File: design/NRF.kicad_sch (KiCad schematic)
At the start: 16 parts, among them U4 nRF24L01P, X2 16M

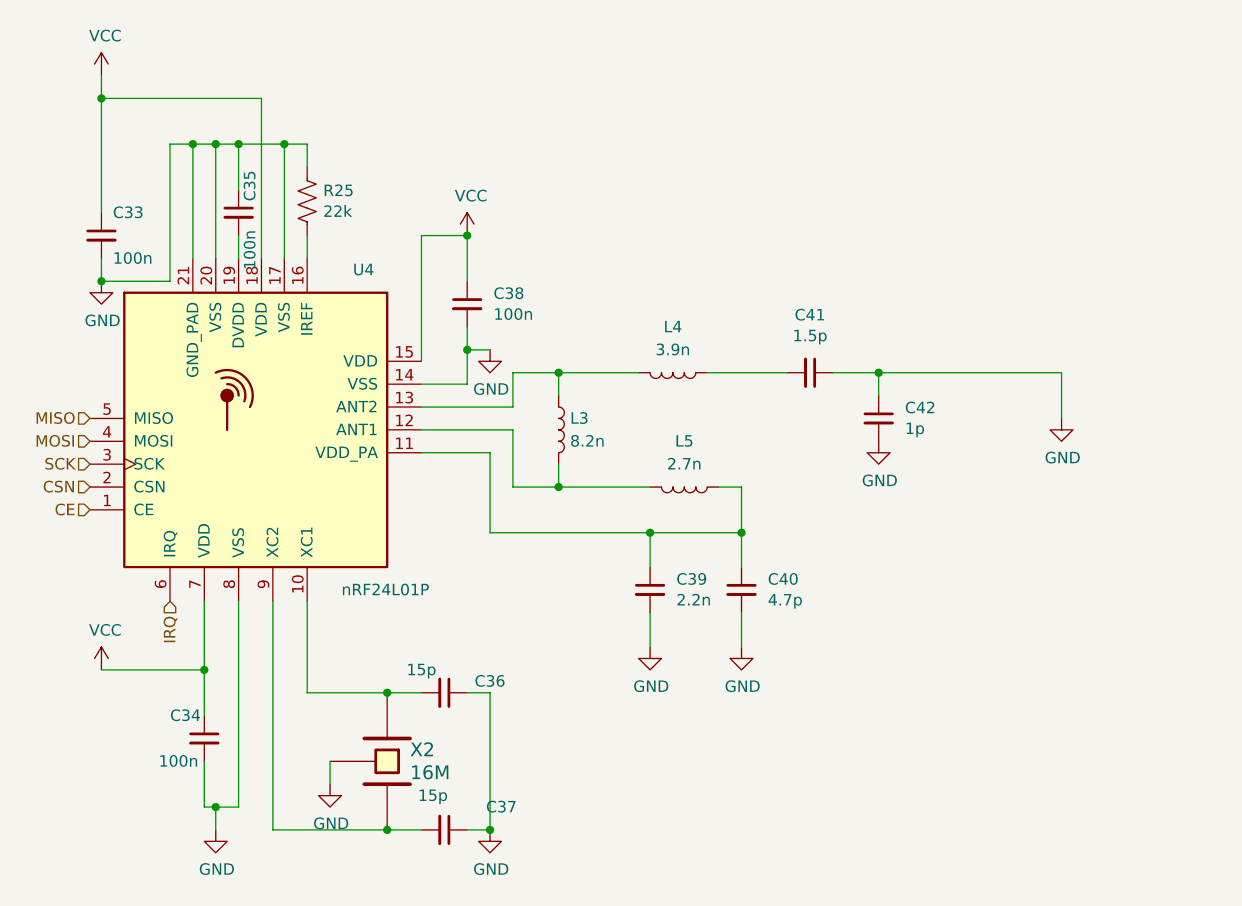
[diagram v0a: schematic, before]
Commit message: Impresión de esquemático en pdf
Impresión de la versión del esquemático en la carpeta /pdf
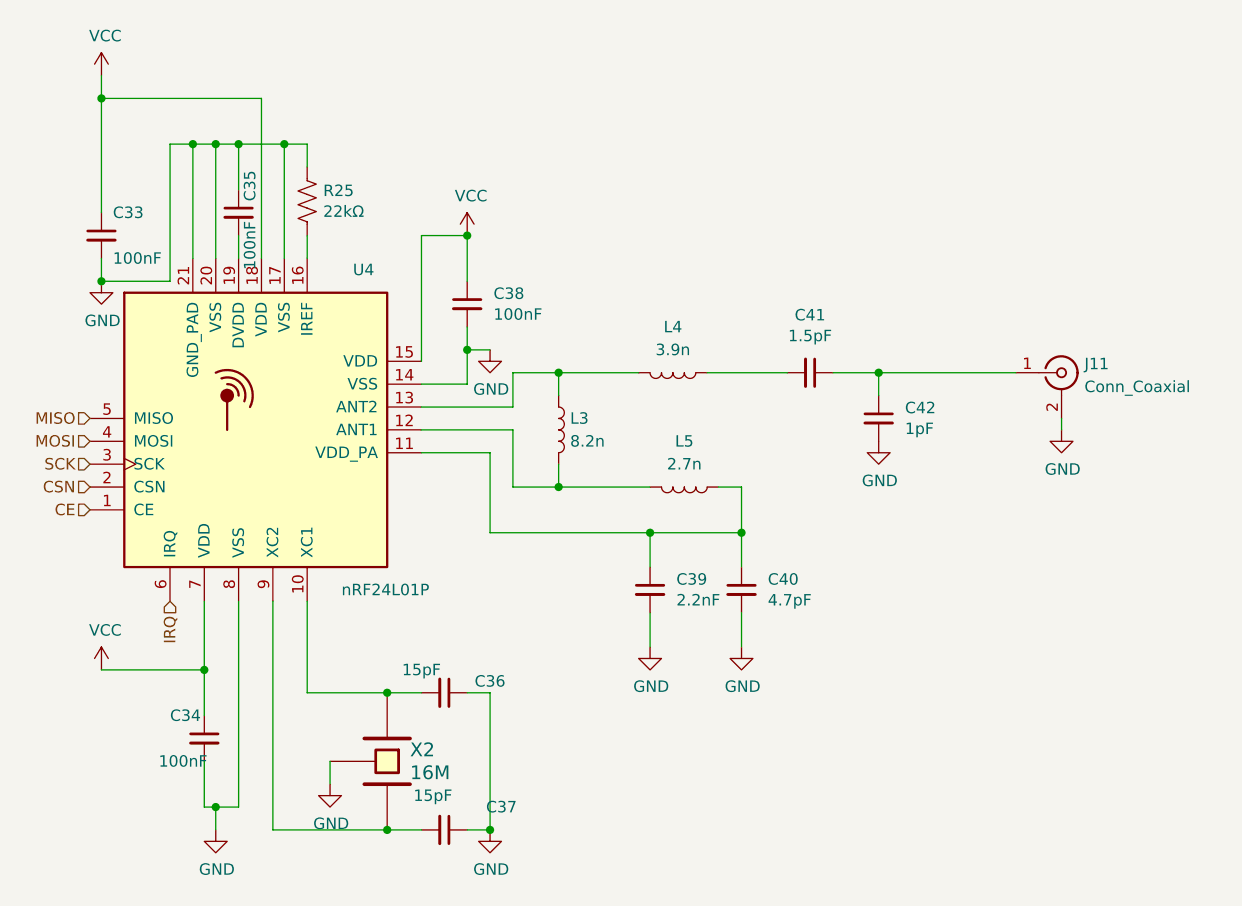
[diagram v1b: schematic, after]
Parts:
- added J11: Conn_Coaxial, symbol Connector:Conn_Coaxial
- C33, C34, C35, C38: value 100n -> 100nF
- C36, C37: value 15p -> 15pF
- C39: value 2.2n -> 2.2nF
- C40: value 4.7p -> 4.7pF
- C41: value 1.5p -> 1.5pF
- C42: value 1p -> 1pF
- R25: value 22k -> 22kΩ
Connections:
- net GND: now also J11.2 (Ext); no longer C41.1, C42.1
- new net: C41.1, C42.1, J11.1 (In)
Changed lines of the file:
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@@
-	(wire
-		(pts
-			(xy 238.76 73.66) (xy 238.76 78.74)
-		)
-		(stroke
-			(width 0)
-			(type default)
-		)
-	)
 	(wire
 		(pts
@@
 	(wire
 		(pts
+			(xy 238.76 80.01) (xy 238.76 78.74)
+		)
+		(stroke
+			(width 0)
+			(type default)
+		)
+	)
+	(wire
+		(pts
 			(xy 152.4 48.26) (xy 154.94 48.26)
 		)
@@
 	(wire
 		(pts
-			(xy 218.44 73.66) (xy 238.76 73.66)
+			(xy 218.44 73.66) (xy 233.68 73.66)
 		)
 		(stroke
@@
 			)
 		)
-		(property "Value" "100n"
+		(property "Value" "100nF"
 			(at 138.43 116.84 0)
 			(effects
@@
 			)
 		)
-		(property "Value" "15p"
+		(property "Value" "15pF"
 			(at 167.64 106.68 90)
 			(effects
@@
 			)
 		)
-		(property "Value" "15p"
+		(property "Value" "15pF"
 			(at 168.91 120.65 90)
 			(effects
@@
 			)
 		)
-		(property "Value" "2.2n"
+		(property "Value" "2.2nF"
 			(at 195.961 98.933 0)
 			(effects
@@
 			)
 		)
-		(property "Description" ""
+		(property "Description" "CAP CER 0603 2.2nF 16V X7R 10%"
 			(at 193.04 97.79 0)
 			(effects
@@
 			)
 		)
-		(property "Value" "4.7p"
+		(property "Value" "4.7pF"
 			(at 206.121 98.933 0)
 			(effects
@@
 			)
 		)
-		(property "Description" ""
+		(property "Description" "CAP CER 0603 4.7PF 16V X7R 10%"
 			(at 203.2 97.79 0)
 			(effects
@@
 			)
 		)
-		(property "Value" "1p"
+		(property "Value" "1pF"
 			(at 221.361 79.883 0)
 			(effects
@@
 			)
 		)
-		(property "Description" ""
+		(property "Description" "CAP CER 0603 1PF 16V X7R 10%"
 			(at 218.44 78.74 0)
 			(effects
@@
 			)
 		)
-		(property "Value" "1.5p"
+		(property "Value" "1.5pF"
 			(at 210.82 69.5706 90)
 			(effects
@@
 			)
 		)
-		(property "Description" ""
+		(property "Description" "CAP CER 0603 1.5PF 16V X7R 10%"
 			(at 210.82 73.66 0)
 			(effects
@@
 			)
 		)
-		(property "Value" "100n"
+		(property "Value" "100nF"
 			(at 175.641 67.183 0)
 			(effects
@@
 			)
 		)
-		(property "Value" "100n"
+		(property "Value" "100nF"
 			(at 133.35 60.96 0)
 			(effects
@@
 			)
 		)
-		(property "Value" "100n"
+		(property "Value" "100nF"
 			(at 148.59 62.23 90)
 			(effects
@@
 			)
 		)
-		(property "Value" "22k"
+		(property "Value" "22kΩ"
 			(at 156.718 55.753 0)
 			(effects
@@
 	(symbol
 		(lib_id "power:GND")
-		(at 238.76 78.74 0)
+		(at 238.76 80.01 0)
 		(unit 1)
 		(exclude_from_sim no)
@@
 		(dnp no)
 		(property "Reference" "#PWR068"
-			(at 238.76 85.09 0)
+			(at 238.76 86.36 0)
 			(effects
 				(font
@@
 		)
 		(property "Value" "GND"
-			(at 238.887 83.1342 0)
+			(at 238.887 84.4042 0)
 			(effects
 				(font
@@
 		)
 		(property "Footprint" ""
-			(at 238.76 78.74 0)
+			(at 238.76 80.01 0)
 			(effects
 				(font
@@
 		)
 		(property "Datasheet" ""
-			(at 238.76 78.74 0)
+			(at 238.76 80.01 0)
 			(effects
 				(font
@@
 		)
 		(property "Description" "Power symbol creates a global label with name \"GND\" , ground"
-			(at 238.76 78.74 0)
+			(at 238.76 80.01 0)
 			(effects
 				(font
@@
 					(unit 1)
 				)
+			)
+		)
+	)
+	(symbol
+		(lib_id "Connector:Conn_Coaxial")
+		(at 238.76 73.66 0)
+		(unit 1)
+		(exclude_from_sim no)
+		(in_bom yes)
+		(on_board yes)
+		(dnp no)
+		(fields_autoplaced yes)
+		(property "Reference" "J11"
+			(at 241.3 72.6831 0)
+			(effects
+				(font
+					(size 1.27 1.27)
+				)
+				(justify left)
+			)
+		)
+		(property "Value" "Conn_Coaxial"
+			(at 241.3 75.2231 0)
+			(effects
+				(font
+					(size 1.27 1.27)
+				)
+				(justify left)
+			)
+		)
+		(property "Footprint" ""
+			(at 238.76 73.66 0)
+			(effects
+				(font
+					(size 1.27 1.27)
+				)
+				(hide yes)
+			)
+		)
+		(property "Datasheet" " ~"
+			(at 238.76 73.66 0)
+			(effects
+				(font
+					(size 1.27 1.27)
+				)
+				(hide yes)
+			)
+		)
+		(property "Description" "coaxial connector (BNC, SMA, SMB, SMC, Cinch/RCA, LEMO, ...)"
+			(at 238.76 73.66 0)
+			(effects
+				(font
+					(size 1.27 1.27)
+				)
+				(hide yes)
+			)
+		)
+		(pin "2"
+		)
+		(pin "1"
+		)
+		(instances
+			(project "ESCX"
+				(path "/6389d757-a1bd-4c0a-9d55-6114b19cc67a/00000000-0000-0000-0000-00005ae4952f"
+					(reference "J11")
+					(unit 1)
+				)

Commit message: Agregado de footprints
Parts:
- L3, L4, L5: footprint (none) -> Inductor_SMD:L_0603_1608Metric_Pad1.05x0.95mm_HandSolder
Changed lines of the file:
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@@
 			)
 		)
-		(property "Description" "CAP 15p, 100V, 0603 "
+		(property "Description" "CAP 15p, 100V, 0603"
 			(at 170.18 109.22 0)
 			(effects
@@
 			)
 		)
-		(property "Description" "CAP 15p, 100V, 0603 "
+		(property "Description" "CAP 15p, 100V, 0603"
 			(at 170.18 124.46 0)
 			(effects
@@
 			)
 		)
-		(property "Footprint" ""
+		(property "Footprint" "Inductor_SMD:L_0603_1608Metric_Pad1.05x0.95mm_HandSolder"
 			(at 182.88 80.01 0)
 			(effects
@@
 			)
 		)
-		(property "Footprint" ""
+		(property "Footprint" "Inductor_SMD:L_0603_1608Metric_Pad1.05x0.95mm_HandSolder"
 			(at 195.58 73.66 0)
 			(effects
@@
 			)
 		)
-		(property "Footprint" ""
+		(property "Footprint" "Inductor_SMD:L_0603_1608Metric_Pad1.05x0.95mm_HandSolder"
 			(at 196.85 86.36 0)
 			(effects
@@
 			)
 		)
-		(property "Datasheet" " ~"
+		(property "Datasheet" "~"
 			(at 238.76 73.66 0)
 			(effects

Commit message: Agrego MFR.Part # a capacitores
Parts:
- C33, C34, C35, C38: Manufacturer (none) -> YAGEO; Manufacturer Product Number  (none) -> CC0603KRX7R9BB104
- C36, C37: Manufacturer (none) -> Samsung Electro-Mechanics; Manufacturer Product Number  (none) -> CL10C150JB8NNNC
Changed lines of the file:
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@@
+			)
+		)
+		(property "Manufacturer" "YAGEO"
+			(at 143.51 114.3 0)
+			(effects
+				(font
+					(size 1.27 1.27)
+				)
+				(hide yes)
+			)
+		)
+		(property "Manufacturer Product Number " "CC0603KRX7R9BB104"
+			(at 143.51 114.3 0)
+			(effects
+				(font
+					(size 1.27 1.27)
+				)
+				(hide yes)
 			)
 		)
@@
 			)
 		)
+		(property "Manufacturer" "Samsung Electro-Mechanics"
+			(at 170.18 109.22 0)
+			(effects
+				(font
+					(size 1.27 1.27)
+				)
+				(hide yes)
+			)
+		)
+		(property "Manufacturer Product Number " "CL10C150JB8NNNC"
+			(at 170.18 109.22 0)
+			(effects
+				(font
+					(size 1.27 1.27)
+				)
+				(hide yes)
+			)
+		)
 		(pin "1"
 		)
@@
 		)
 		(property "Description" "CAP 15p, 100V, 0603"
+			(at 170.18 124.46 0)
+			(effects
+				(font
+					(size 1.27 1.27)
+				)
+				(hide yes)
+			)
+		)
+		(property "Manufacturer" "Samsung Electro-Mechanics"
+			(at 170.18 124.46 0)
+			(effects
+				(font
+					(size 1.27 1.27)
+				)
+				(hide yes)
+			)
+		)
+		(property "Manufacturer Product Number " "CL10C150JB8NNNC"
 			(at 170.18 124.46 0)
 			(effects
@@
 			)
 		)
+		(property "Manufacturer" "YAGEO"
+			(at 172.72 66.04 0)
+			(effects
+				(font
+					(size 1.27 1.27)
+				)
+				(hide yes)
+			)
+		)
+		(property "Manufacturer Product Number " "CC0603KRX7R9BB104"
+			(at 172.72 66.04 0)
+			(effects
+				(font
+					(size 1.27 1.27)
+				)
+				(hide yes)
+			)
+		)
 		(pin "2"
 		)
@@
 			)
 		)
+		(property "Manufacturer" "YAGEO"
+			(at 132.08 58.42 0)
+			(effects
+				(font
+					(size 1.27 1.27)
+				)
+				(hide yes)
+			)
+		)
+		(property "Manufacturer Product Number " "CC0603KRX7R9BB104"
+			(at 132.08 58.42 0)
+			(effects
+				(font
+					(size 1.27 1.27)
+				)
+				(hide yes)
+			)
+		)
 		(pin "1"
 		)
@@
 			(at 147.32 55.88 0)
 			(effects
+				(font
+					(size 1.27 1.27)
+				)
+				(hide yes)
+			)
+		)
+		(property "Manufacturer" "YAGEO"
+			(at 147.32 55.88 0)
+			(effects
+				(font
+					(size 1.27 1.27)
+				)
+				(hide yes)
+			)
+		)
+		(property "Manufacturer Product Number " "CC0603KRX7R9BB104"
+			(at 147.32 55.88 0)
+			(effects

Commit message: Agregue Manufacturer Product Numbers
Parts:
- C39: Manufacturer (none) -> FH (Guangdong Fenghua Advanced Tech); Manufacturer Product Number  (none) -> 0603B222K500NT
- C40: Manufacturer (none) -> Samsung Electro-Mechanics; Manufacturer Product Number  (none) -> CL10C4R7BB8NNNC
- C41: Manufacturer (none) -> YAGEO; Manufacturer Product Number  (none) -> AC0603BRNPO9BN1R5
- C42: Manufacturer (none) -> YAGEO; Manufacturer Product Number  (none) -> CC0603CRNPO8BN1R0
- L3: Manufacturer (none) -> Murata Electronics; Manufacturer Product Number  (none) -> LQW18AS8N2G00D
- L4: Manufacturer (none) -> KYOCERA AVX; Manufacturer Product Number  (none) -> LCCI0603S3N9GTAR
- L5: Manufacturer (none) -> Pulse Electronics; Manufacturer Product Number  (none) -> BSCH001608082N7S00
- R25: Manufacturer (none) -> YAGEO; Manufacturer Product Number  (none) -> RC0603JR-0722KL
- U4: Manufacturer (none) -> Nordic Semiconductor ASA; Manufacturer Product Number  (none) -> NRF24L01P-R
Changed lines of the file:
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@@
+			)
+		)
+		(property "Manufacturer" "Nordic Semiconductor ASA"
+			(at 146.05 81.28 0)
+			(effects
+				(font
+					(size 1.27 1.27)
+				)
+				(hide yes)
+			)
+		)
+		(property "Manufacturer Product Number " "NRF24L01P-R"
+			(at 146.05 81.28 0)
+			(effects
+				(font
+					(size 1.27 1.27)
+				)
+				(hide yes)
 			)
 		)
@@
 			)
 		)
+		(property "Manufacturer" "Murata Electronics"
+			(at 182.88 80.01 0)
+			(effects
+				(font
+					(size 1.27 1.27)
+				)
+				(hide yes)
+			)
+		)
+		(property "Manufacturer Product Number " "LQW18AS8N2G00D"
+			(at 182.88 80.01 0)
+			(effects
+				(font
+					(size 1.27 1.27)
+				)
+				(hide yes)
+			)
+		)
 		(pin "2"
 		)
@@
 			)
 		)
+		(property "Manufacturer" " KYOCERA AVX"
+			(at 195.58 73.66 0)
+			(effects
+				(font
+					(size 1.27 1.27)
+				)
+				(hide yes)
+			)
+		)
+		(property "Manufacturer Product Number " "LCCI0603S3N9GTAR"
+			(at 195.58 73.66 0)
+			(effects
+				(font
+					(size 1.27 1.27)
+				)
+				(hide yes)
+			)
+		)
 		(pin "2"
 		)
@@
 			)
 		)
+		(property "Manufacturer" " Pulse Electronics"
+			(at 196.85 86.36 0)
+			(effects
+				(font
+					(size 1.27 1.27)
+				)
+				(hide yes)
+			)
+		)
+		(property "Manufacturer Product Number " "BSCH001608082N7S00"
+			(at 196.85 86.36 0)
+			(effects
+				(font
+					(size 1.27 1.27)
+				)
+				(hide yes)
+			)
+		)
 		(pin "1"
 		)
@@
 			)
 		)
+		(property "Manufacturer" "FH (Guangdong Fenghua Advanced Tech)"
+			(at 193.04 97.79 0)
+			(effects
+				(font
+					(size 1.27 1.27)
+				)
+				(hide yes)
+			)
+		)
+		(property "Manufacturer Product Number " "0603B222K500NT"
+			(at 193.04 97.79 0)
+			(effects
+				(font
+					(size 1.27 1.27)
+				)
+				(hide yes)
+			)
+		)
 		(pin "1"
 		)
@@
 			)
 		)
+		(property "Manufacturer" "Samsung Electro-Mechanics"
+			(at 203.2 97.79 0)
+			(effects
+				(font
+					(size 1.27 1.27)
+				)
+				(hide yes)
+			)
+		)
+		(property "Manufacturer Product Number " "CL10C4R7BB8NNNC"
+			(at 203.2 97.79 0)
+			(effects
+				(font
+					(size 1.27 1.27)
+				)
+				(hide yes)
+			)
+		)
 		(pin "1"
 		)
@@
 			)
 		)
+		(property "Manufacturer" "YAGEO"
+			(at 218.44 78.74 0)
+			(effects
+				(font
+					(size 1.27 1.27)
+				)
+				(hide yes)
+			)
+		)
+		(property "Manufacturer Product Number " "CC0603CRNPO8BN1R0"
+			(at 218.44 78.74 0)
+			(effects
+				(font
+					(size 1.27 1.27)
+				)
+				(hide yes)
+			)
+		)
 		(pin "1"
 		)
@@
 			)
 		)
+		(property "Manufacturer" "YAGEO"
+			(at 210.82 73.66 0)
+			(effects
+				(font
+					(size 1.27 1.27)
+				)
+				(hide yes)
+			)
+		)
+		(property "Manufacturer Product Number " "AC0603BRNPO9BN1R5"
+			(at 210.82 73.66 0)
+			(effects
+				(font
+					(size 1.27 1.27)
+				)
+				(hide yes)
+			)
+		)
 		(pin "1"
 		)
@@
 			(at 154.94 54.61 0)
 			(effects
+				(font
+					(size 1.27 1.27)
+				)
+				(hide yes)
+			)
+		)
+		(property "Manufacturer" "YAGEO"
+			(at 154.94 54.61 0)
+			(effects
+				(font
+					(size 1.27 1.27)
+				)
+				(hide yes)
+			)
+		)
+		(property "Manufacturer Product Number " "RC0603JR-0722KL"
+			(at 154.94 54.61 0)
+			(effects

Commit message: Agregue Manufacturer Product Number
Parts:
- removed C37: 15pF, Capacitor_SMD:C_0603_1608Metric, symbol Device:C_Small
- removed X2: 16M, symbol ESCX-cache:crf_1{colon}CRYSTAL_GROUND_PIN
- added C36: 15pF, Capacitor_SMD:C_0603_1608Metric, symbol Device:C_Small
- added X2: 16MHz, Crystal:Crystal_SMD_HC49-SD, symbol Device:Crystal_Small
- J4: renamed from J11; footprint (none) -> Connector_Coaxial:SMA_Amphenol_901-143_Horizontal
- renumbered C33 to C32, C34 to C33, C35 to C34, C36 to C35, C38 to C37, C39 to C38, C40 to C39, C41 to C40, C42 to C41, R25 to R27
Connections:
- net GND: now also C36.1
- net at C35.2, U4.10 (XC1): now also X2.2
- net at U4.9 (XC2): now also C36.2, X2.1
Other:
- moved on the sheet: C35

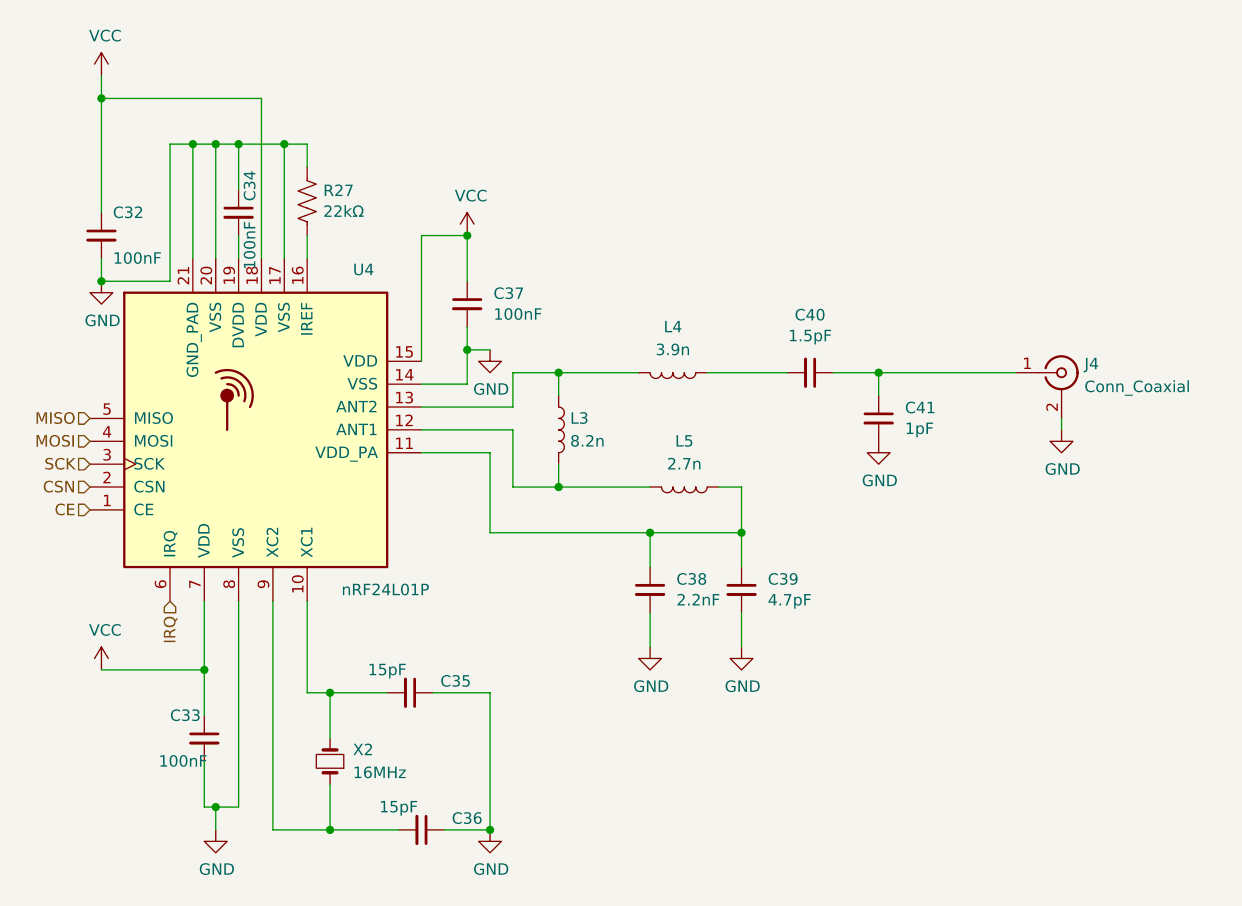
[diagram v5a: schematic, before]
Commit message: Ordenado del esquemático
- Cambios en los capacitores del oscilador
- Mejora de los esquemáticos, encapsulado la interfáz usb y los sensores del motor
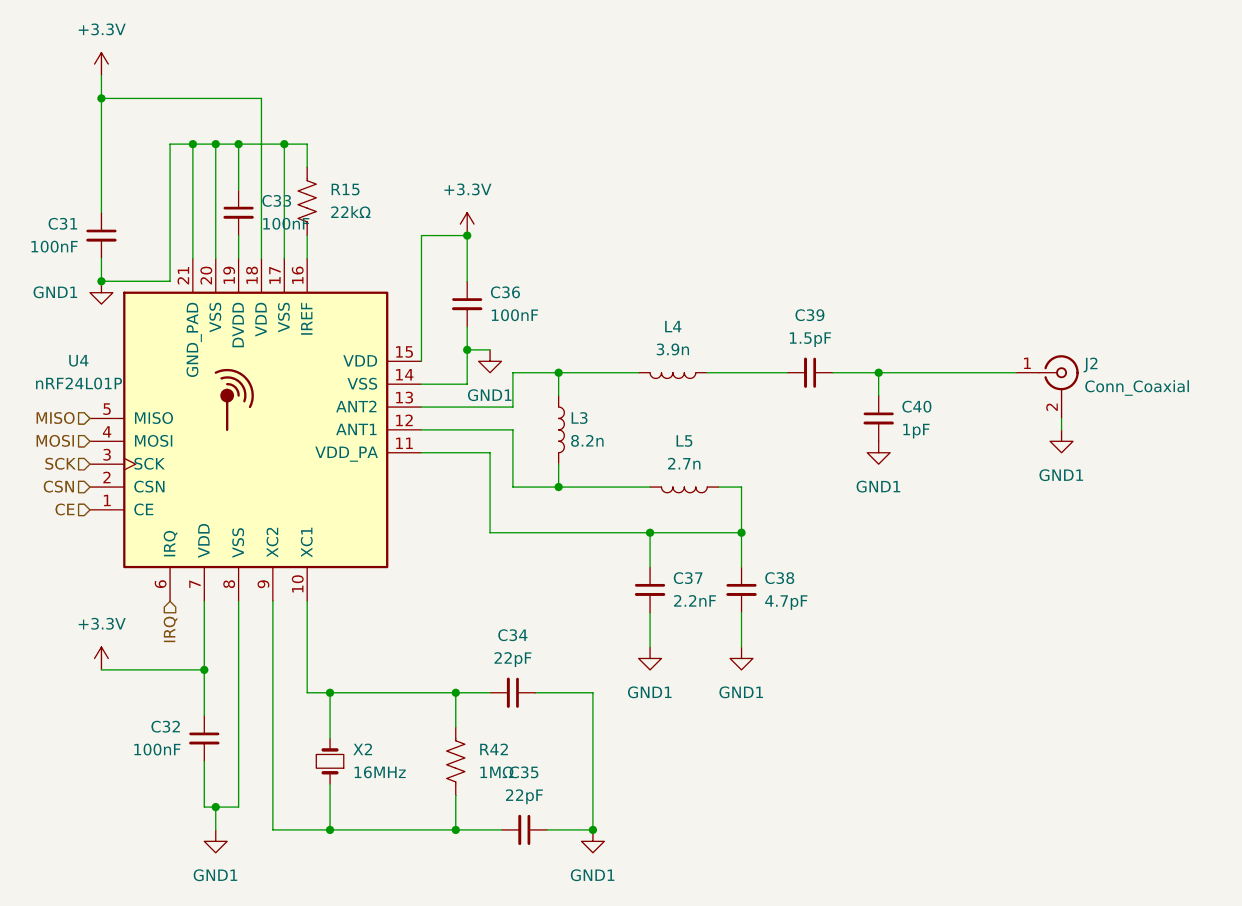
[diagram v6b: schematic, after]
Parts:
- added R42: 1MΩ, Resistor_SMD:R_0603_1608Metric, symbol Device:R_US
- C34: renamed from C35; value 15pF -> 22pF
- C35: renamed from C36; value 15pF -> 22pF
- renumbered C32 to C31, C33 to C32, C34 to C33, C37 to C36, C38 to C37, C39 to C38, C40 to C39, C41 to C40, J4 to J2, R27 to R15
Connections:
- net at C34.2, U4.10 (XC1), X2.2: now also R42.1
- net at C35.2, U4.9 (XC2), X2.1: now also R42.2
- net GND renamed GND1
- net VCC renamed +3.3V
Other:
- moved on the sheet: C34, C35
